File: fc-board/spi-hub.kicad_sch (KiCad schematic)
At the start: 7 parts, among them U10 LTC2983ILX-PBF

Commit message: FC board updates
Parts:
- added C21, C22, C23, C24: 10n, Capacitor_SMD:C_1206_3216Metric, symbol Device:C_Small
- added J14: BCS-110-L-D-TE, fc-board:SAMTEC_BCS-110-L-D-TE, symbol fc-board:BCS-110-L-D-TE
- added R38: 5k, Resistor_SMD:R_1206_3216Metric, symbol Device:R_Small
- added R39: PTS0805M1B500RP100, fc-board:PTS0805M1B500RP100, symbol fc-board:PTS0805M1B500RP100
- C18: renamed from C25; footprint (none) -> Capacitor_SMD:C_1206_3216Metric
- C19: renamed from C26; footprint (none) -> Capacitor_SMD:C_1206_3216Metric
- C20: renamed from C24; footprint (none) -> Capacitor_SMD:C_1206_3216Metric
- renumbered C22 to C15, C23 to C16, C21 to C17
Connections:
- net GND: now also C21.2, C22.2, C23.2, C24.2
- net CH1: now reaches U10.16 (CH1)
- net CH1: now also J14.01
- net CH2: now reaches U10.17 (CH2)
- net CH2: now also J14.02
- net CH3: now reaches U10.18 (CH3)
- net CH3: now also J14.03
- net CH4: now reaches U10.19 (CH4)
- net CH4: now also J14.04
- net CH5: now reaches U10.20 (CH5)
- net CH5: now also J14.05
- net CH6: now reaches U10.21 (CH6)
- net CH6: now also J14.06
- net CH7: now reaches U10.22 (CH7)
- net CH7: now also J14.07
- net CH8: now reaches U10.23 (CH8)
- net CH8: now also J14.08
- net CH9: now reaches U10.24 (CH9)
- net CH9: now also J14.09
- net CH10: now reaches U10.25 (CH10)
- net CH10: now also J14.10
- net CH11: now reaches U10.26 (CH11)
- net CH11: now also J14.11
- net CH12: now reaches U10.27 (CH12)
- net CH12: now also J14.12
- net CH13: now reaches U10.28 (CH13)
- net CH13: now also J14.13
- net CH14: now reaches U10.29 (CH14)
- net CH14: now also J14.14
- net CH15: now reaches U10.30 (CH15)
- net CH15: now also J14.15
- net CH16: now reaches U10.31 (CH16)
- net CH16: now also J14.16
- net CH17: now reaches U10.32 (CH17)
- net CH17: now also C22.1, J14.17, R38.1
- net CH18: now reaches U10.33 (CH18)
- net CH18: now also U10.34 (CH19), C21.1, C24.1, J14.18, J14.19, R38.2, R39.2
- net CH20: now reaches U10.35 (CH20)
- net CH20: now also C23.1, J14.20, R39.1
- net CS renamed CS_LTC2983
- net INTERRUPT renamed INTERRUPT_LTC2983
- net RESET renamed RESET_LTC2983
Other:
- note added: "ADD DIODE FOR TEMPERATURE COMPENSATION"
- note added: "ADD RESISTORS AND CAPACITORS TO THERMOCOUPLE CHANNELS"
- note added: "Sense resistor"
- moved on the sheet: C15, C16, C17, C18, C19, C20

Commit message: Finished routing; cleaned library
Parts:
- added JP10: CH3to20, Jumper:SolderJumper-2_P1.3mm_Open_Pad1.0x1.5mm, symbol Jumper:SolderJumper_2_Open
- added JP11: CH5to20, Jumper:SolderJumper-2_P1.3mm_Open_Pad1.0x1.5mm, symbol Jumper:SolderJumper_2_Open
- added JP12: CH7to20, Jumper:SolderJumper-2_P1.3mm_Open_Pad1.0x1.5mm, symbol Jumper:SolderJumper_2_Open
- added JP13: CH9to20, Jumper:SolderJumper-2_P1.3mm_Open_Pad1.0x1.5mm, symbol Jumper:SolderJumper_2_Open
- added JP14: CH11to20, Jumper:SolderJumper-2_P1.3mm_Open_Pad1.0x1.5mm, symbol Jumper:SolderJumper_2_Open
- added JP15: CH13to20, Jumper:SolderJumper-2_P1.3mm_Open_Pad1.0x1.5mm, symbol Jumper:SolderJumper_2_Open
- added JP16: CH15to20, Jumper:SolderJumper-2_P1.3mm_Open_Pad1.0x1.5mm, symbol Jumper:SolderJumper_2_Open
- added JP9: CH1to20, Jumper:SolderJumper-2_P1.3mm_Open_Pad1.0x1.5mm, symbol Jumper:SolderJumper_2_Open
- R37: renamed from R38; value 5k -> 5k, temp stable
- renumbered C15 to C17, C16 to C18, C17 to C19, C18 to C20, C19 to C21, C20 to C22, C22 to C23, C21 to C24, C23 to C25, C24 to C26, J14 to J15, R39 to R38
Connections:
- net CH1: now also JP9.1 (A)
- net CH11: now also JP14.1 (A)
- net CH13: now also JP15.1 (A)
- net CH15: now also JP16.1 (A)
- net CH17: now also C24.1, C26.1, J15.20, R37.2, R38.2, U10.35 (CH20), JP10.2 (B), JP11.2 (B), JP12.2 (B), JP13.2 (B), JP14.2 (B), JP15.2 (B), JP16.2 (B), JP9.2 (B); no longer C23.1, R37.1
- net CH18: now also C25.1, R38.1; no longer C24.1, C26.1, J15.19, R37.2, R38.2, U10.34 (CH19)
- net CH3: now also JP10.1 (A)
- net CH5: now also JP11.1 (A)
- net CH7: now also JP12.1 (A)
- net CH9: now also JP13.1 (A)
- removed net CH20: C25.1, J15.20, R38.1, U10.35 (CH20)
- net VDD renamed 3.3V
- new net CH19: C23.1, J15.19, R37.1, U10.34 (CH19)
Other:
- note added: "Jump to RTD sense resistor"
- note added: "RTD for thermocouple cold junction compensation"
- note added: "RTD sense resistor"
- note added: "This effectively allows us to switch between using thermocouples and RTDs"
- note added: "Ultra temperature stable"
- note removed: "Sense resistor"
- moved on the sheet: C19, C23, C24, C25, C26, R37, R38

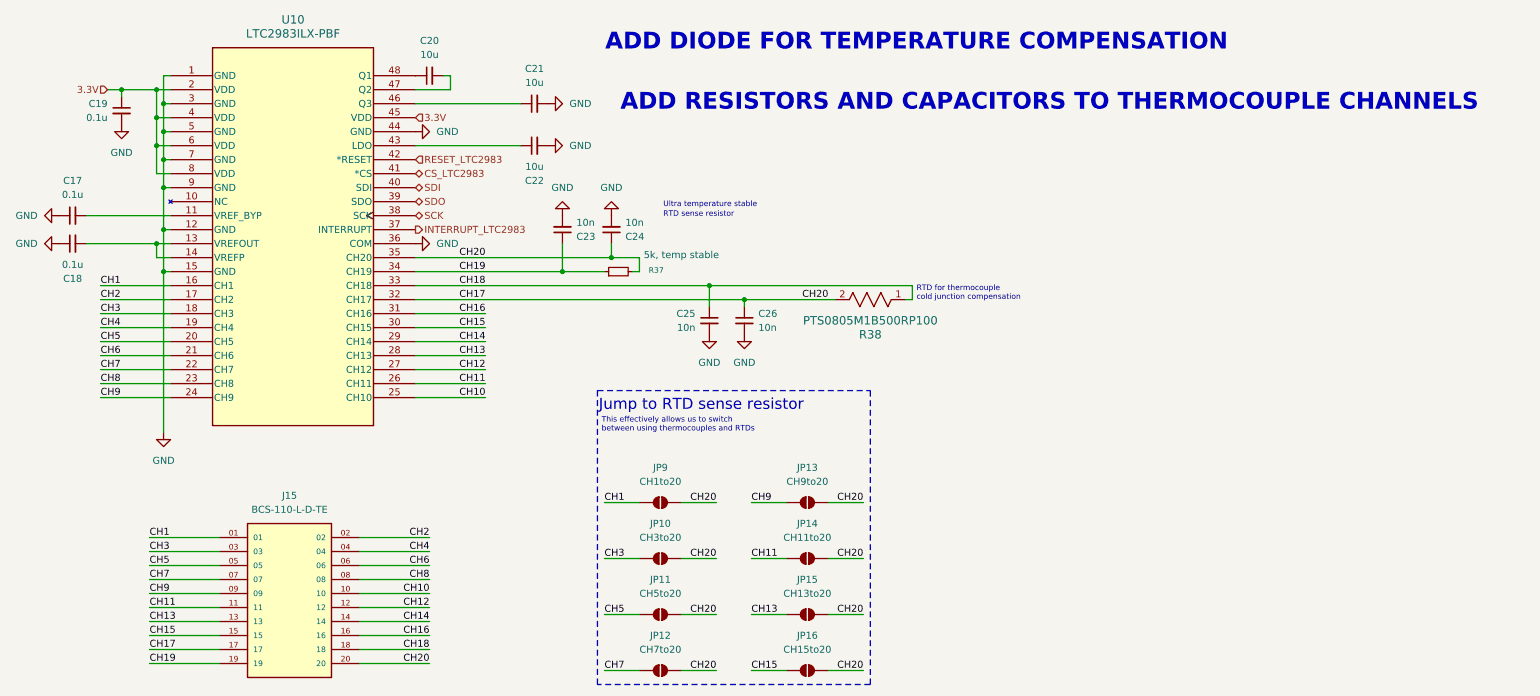
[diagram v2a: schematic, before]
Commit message: Updated RJ45 jack
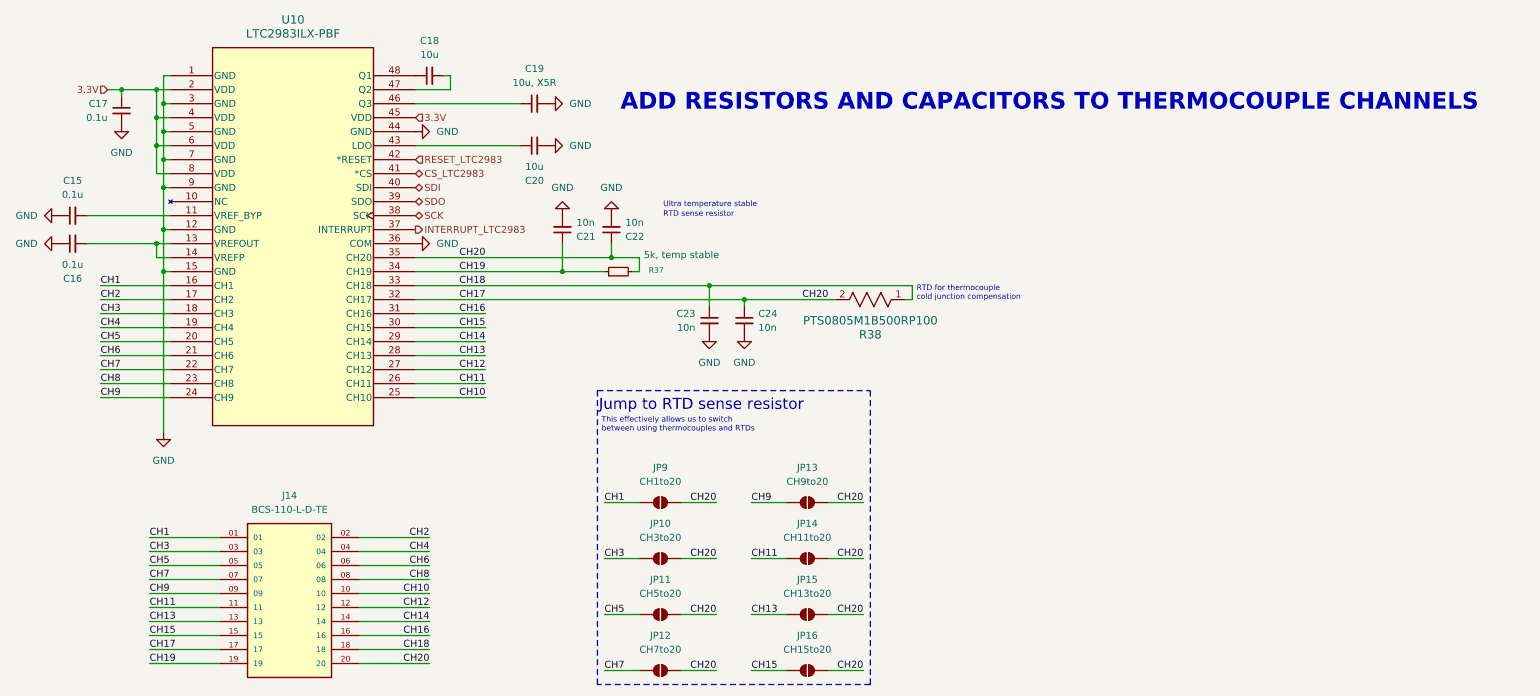
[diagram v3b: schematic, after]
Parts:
- C19: renamed from C21; value 10u -> 10u, X5R
- renumbered C17 to C15, C18 to C16, C19 to C17, C20 to C18, C22 to C20, C23 to C21, C24 to C22, C25 to C23, C26 to C24, J15 to J14
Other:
- note removed: "ADD DIODE FOR TEMPERATURE COMPENSATION"

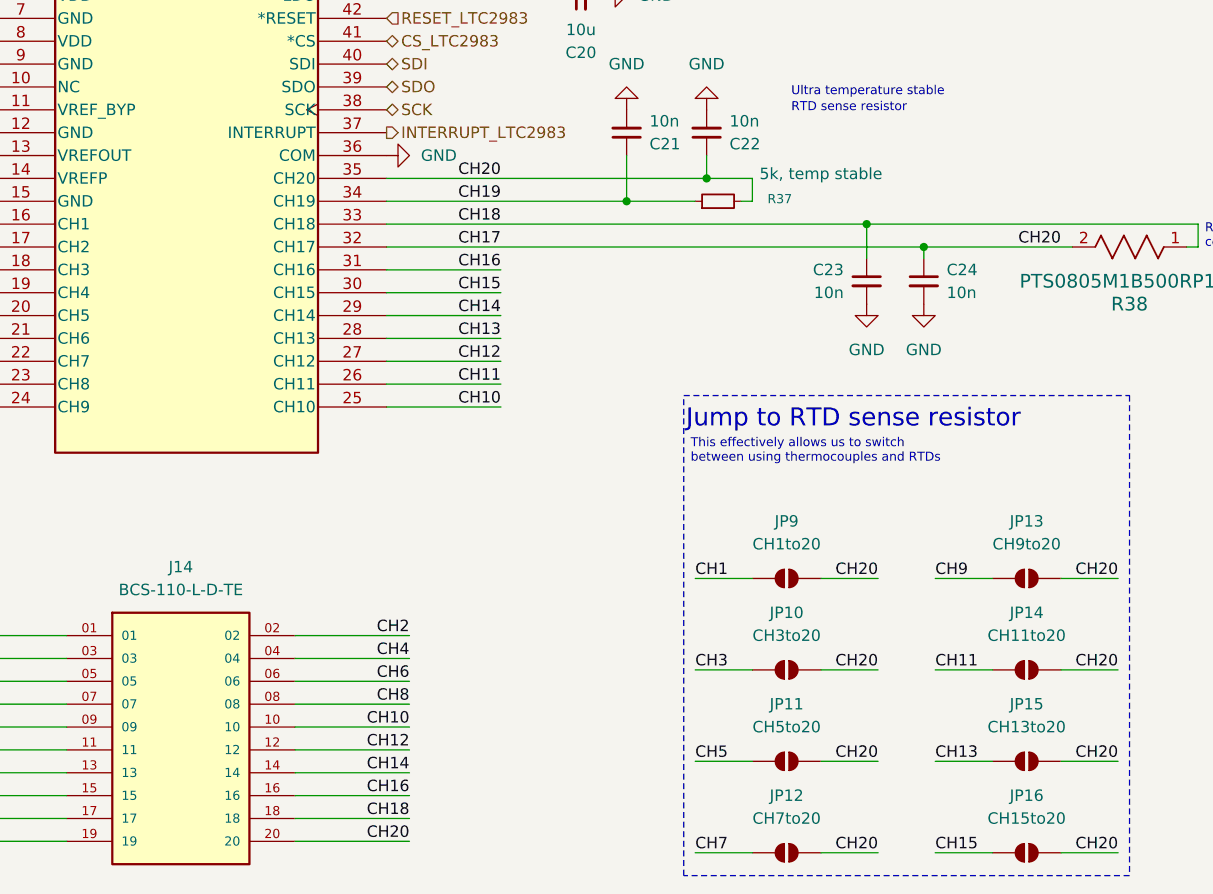
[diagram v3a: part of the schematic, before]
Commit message: Assigned part numbers to everything, replaced ethernet jack
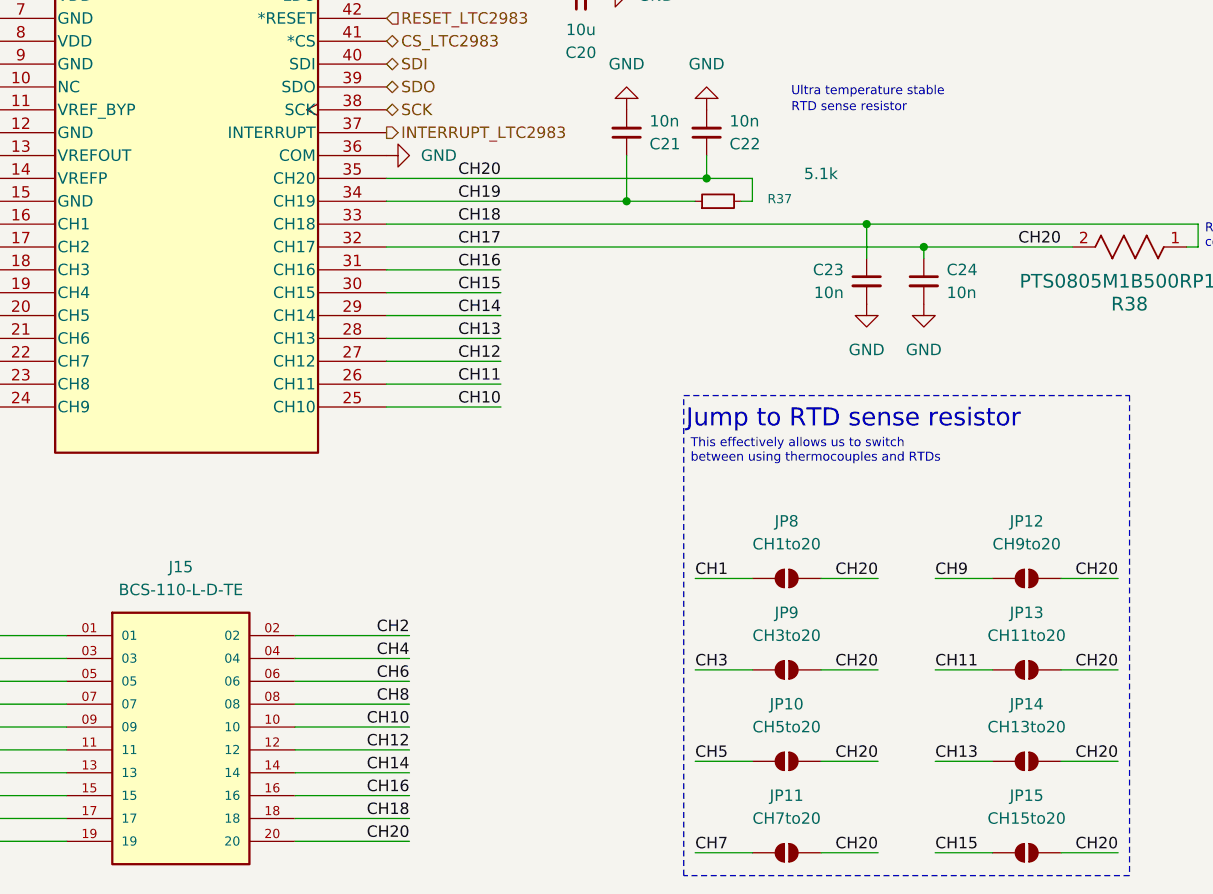
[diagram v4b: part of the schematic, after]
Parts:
- R37: value 5k, temp stable -> 5.1k
- renumbered J14 to J15, JP11 to JP10, JP12 to JP11, JP13 to JP12, JP14 to JP13, JP15 to JP14, JP16 to JP15, JP9 to JP8, JP10 to JP9

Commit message: Finalized layout
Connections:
- net CH1: now also J15.1; no longer J15.01
- net CH2: now also J15.2; no longer J15.02
- net CH3: now also J15.3; no longer J15.03
- net CH4: now also J15.4; no longer J15.04
- net CH5: now also J15.5; no longer J15.05
- net CH6: now also J15.6; no longer J15.06
- net CH7: now also J15.7; no longer J15.07
- net CH8: now also J15.8; no longer J15.08
- net CH9: now also J15.9; no longer J15.09
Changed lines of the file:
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@@
 		(pin "13"
 		)
-		(pin "09"
+		(pin "1"
 		)
-		(pin "02"
+		(pin "4"
 		)
 		(pin "14"
 		)
-		(pin "04"
+		(pin "7"
 		)
 		(pin "15"
 		)
-		(pin "07"
+		(pin "8"
 		)
-		(pin "08"
+		(pin "9"
 		)
-		(pin "03"
+		(pin "3"
 		)
-		(pin "01"
+		(pin "6"
 		)
 		(pin "11"
@@
 		(pin "20"
 		)
-		(pin "05"
+		(pin "2"
 		)
 		(pin "18"
@@
 		(pin "19"
 		)
-		(pin "06"
+		(pin "5"
 		)
 		(pin "12"
